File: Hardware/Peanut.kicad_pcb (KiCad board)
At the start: 2 copper layers, 92 x 44 mm, 54 parts, among them J1 BL602 Female JST Connector, J2 Extension Male JST Connector, J3 AudioPlug3, Q1 Q_NPN_BEC, SW1 Push_Button, SW2 Push_Button, SW3 Push_Button, SW4 Push_Button, SW5 Slide Switch, SW6 Slide Switch, U1 BNO085, U2 PCF8574APWR, U3 HDC2010YPAR, U4 LTR-303ALS-01, U5 MCP4728T-E/UN, U6 LWP040-PSGLC-S, U7 ADS1015IDGSR, U8 INA350ABSIDDFR, Y1 Crystal_32.768kHz

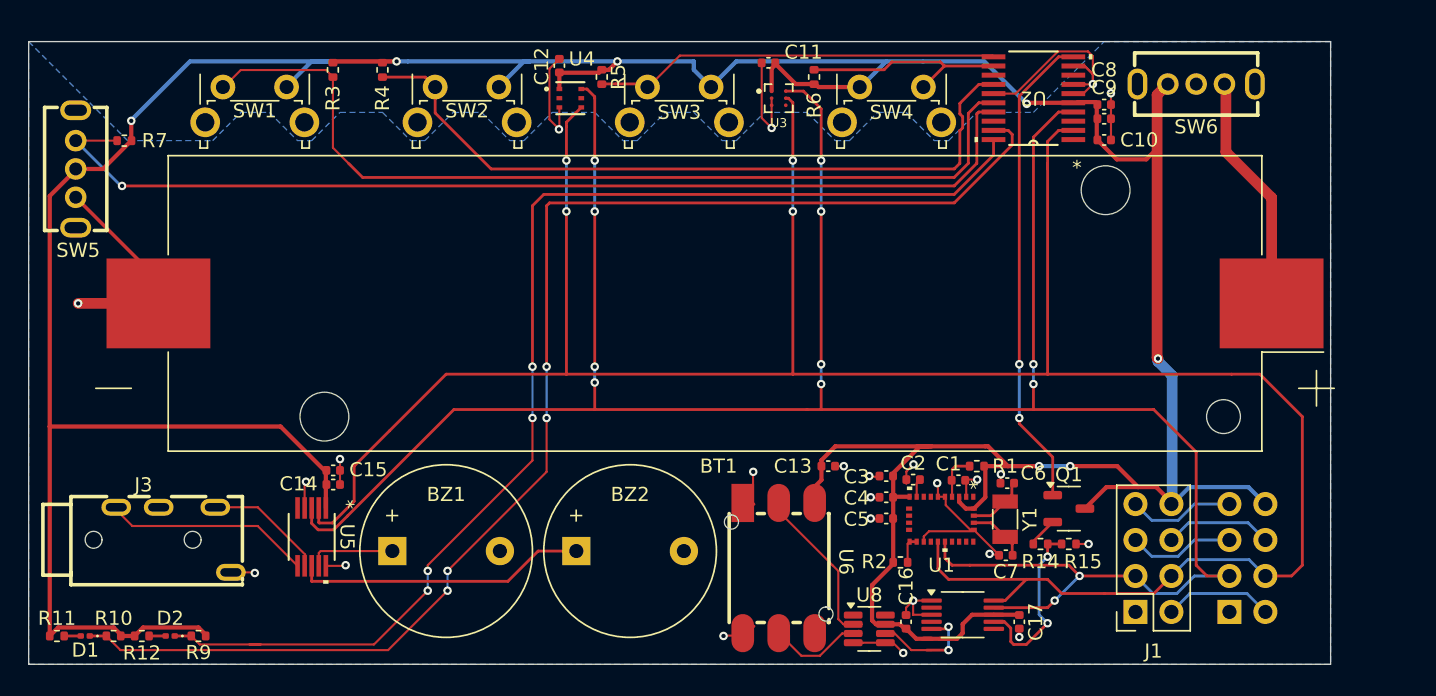
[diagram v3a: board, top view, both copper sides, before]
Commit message: Updates to PCB and ADC Schematics
- Swapped audio jack to correct pin (4P-DIP)
- Add LCSC numbers for all components
- Reroute some sensitive signal traces
- Add Board rev and author
- add 4x M2 mounting holes
- fixup some misc silkscreen, footprints, and component 3d models
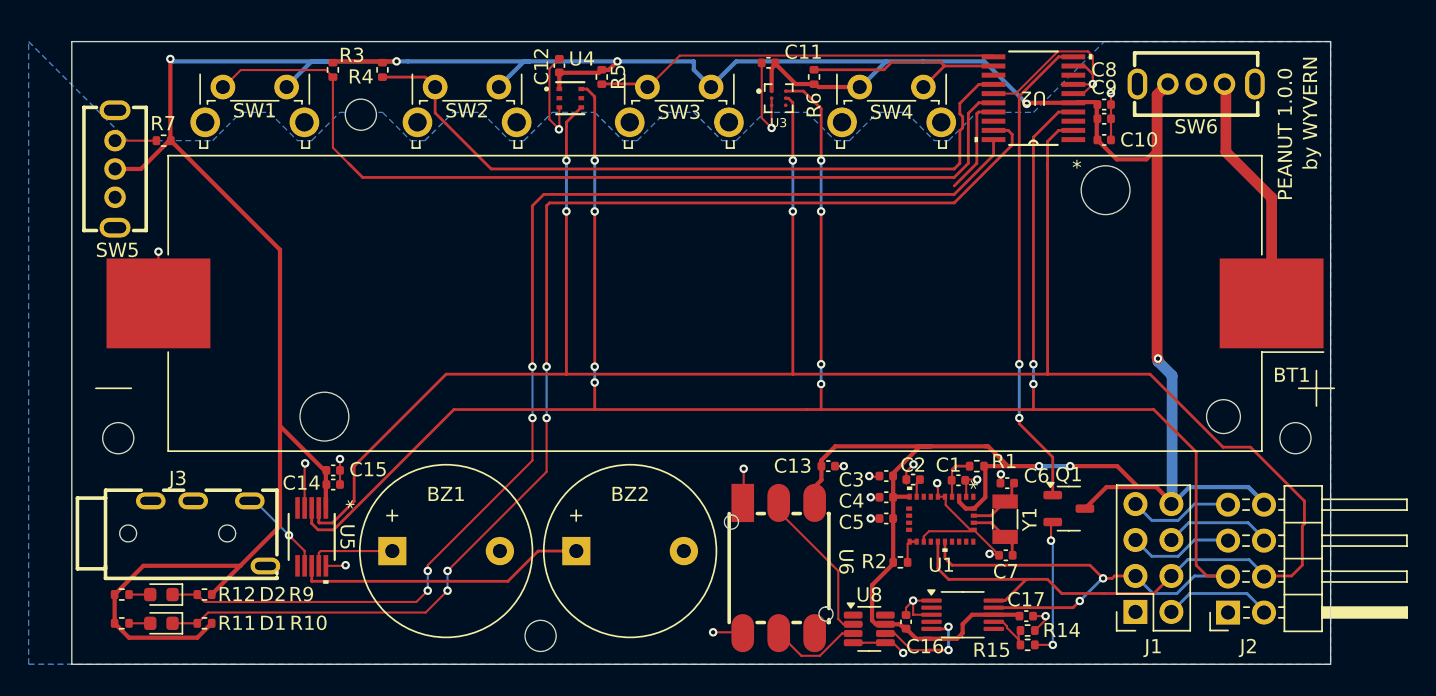
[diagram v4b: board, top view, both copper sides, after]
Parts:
- added REF**: MountingHole_2.2mm_M2_DIN965, MountingHole:MountingHole_2.2mm_M2_DIN965, F.Cu at (117.5, 50.2)
- added REF**: MountingHole_2.2mm_M2_DIN965, MountingHole:MountingHole_2.2mm_M2_DIN965, F.Cu at (183.5, 73.0)
- added REF**: MountingHole_2.2mm_M2_DIN965, MountingHole:MountingHole_2.2mm_M2_DIN965, F.Cu at (100.3, 73.0)
- added REF**: MountingHole_2.2mm_M2_DIN965, MountingHole:MountingHole_2.2mm_M2_DIN965, F.Cu at (130.2, 87.0)
- D1: footprint LED_SMD:LED_0201_0603Metric -> LED_SMD:LED_0603_1608Metric
- D2: value GRN -> YELLOW; footprint LED_SMD:LED_0201_0603Metric -> LED_SMD:LED_0603_1608Metric
- J2: moved to F.Cu
- moved J2 7.58 mm to (178.8, 77.7)
- moved R14 7.19 mm to (164.6, 87.6), turned to 180 degrees
- moved R15 6.77 mm to (164.6, 86.6)
- moved R10 6.49 mm to (106.4, 86.1)
- moved D1 5.45 mm to (103.4, 86.1)
- moved R11 4.67 mm to (100.6, 86.1)
- moved R12 3.25 mm to (100.6, 84.1)
- moved D2 2.99 mm to (103.4, 84.1)
- moved R9 2.96 mm to (106.4, 84.1)
- moved R7 2.78 mm to (103.5, 52.0)
- moved SW5 2.78 mm to (100.1, 54.0)
- moved J3 2.48 mm to (106.7, 79.8)
- moved C17 0.64 mm to (164.5, 85.6), turned to 0 degrees
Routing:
- net Net-(U2-P5): track 73.1 -> 9.67 mm, vias 1 -> 0
- net Net-(U5-VOUTA): track 14.6 -> 0.00 mm
- net GND: track 94.1 -> 84.1 mm, vias 24 -> 22
- net Net-(U7-AIN3): track 12.9 -> 2.88 mm, vias 2 -> 0
- net Net-(Q1-E): track 2.12 -> 9.96 mm, vias 0 -> 2
- net Net-(D1-K): track 94.5 -> 87.5 mm
- net +3V3: track 294.0 -> 288.6 mm
- net SCL: track 179.3 -> 176.0 mm
- net Net-(D2-K): track 86.1 -> 84.1 mm
- net Net-(U5-VOUTB): track 8.27 -> 6.39 mm, vias 0 -> 1
- net SDA: track 179.4 -> 181.1 mm
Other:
- board size 92 x 44 mm -> 89 x 44 mm
- board text added: "PEANUT 1.0.0"
- board text added: "by WYVERN"
